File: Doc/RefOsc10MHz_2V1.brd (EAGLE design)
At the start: 90 x 70 mm, 77 parts, among them CON1 TYCO-AMP_USBUSB-B_SMT, CON11 MCX-J-P-X-RA-SM1, CON2 HEADER-2X5SMD, CON3 SD-73100-0105, CON4 AVR-ISP-6SMD, CON5 AVR-JTAG-10SMD, CON6 HEADER-2X3SMD, IC1 ATmega328-P, IC11 712-RXM-GNSS-TM-B, IC2 LC4032V_XXT44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

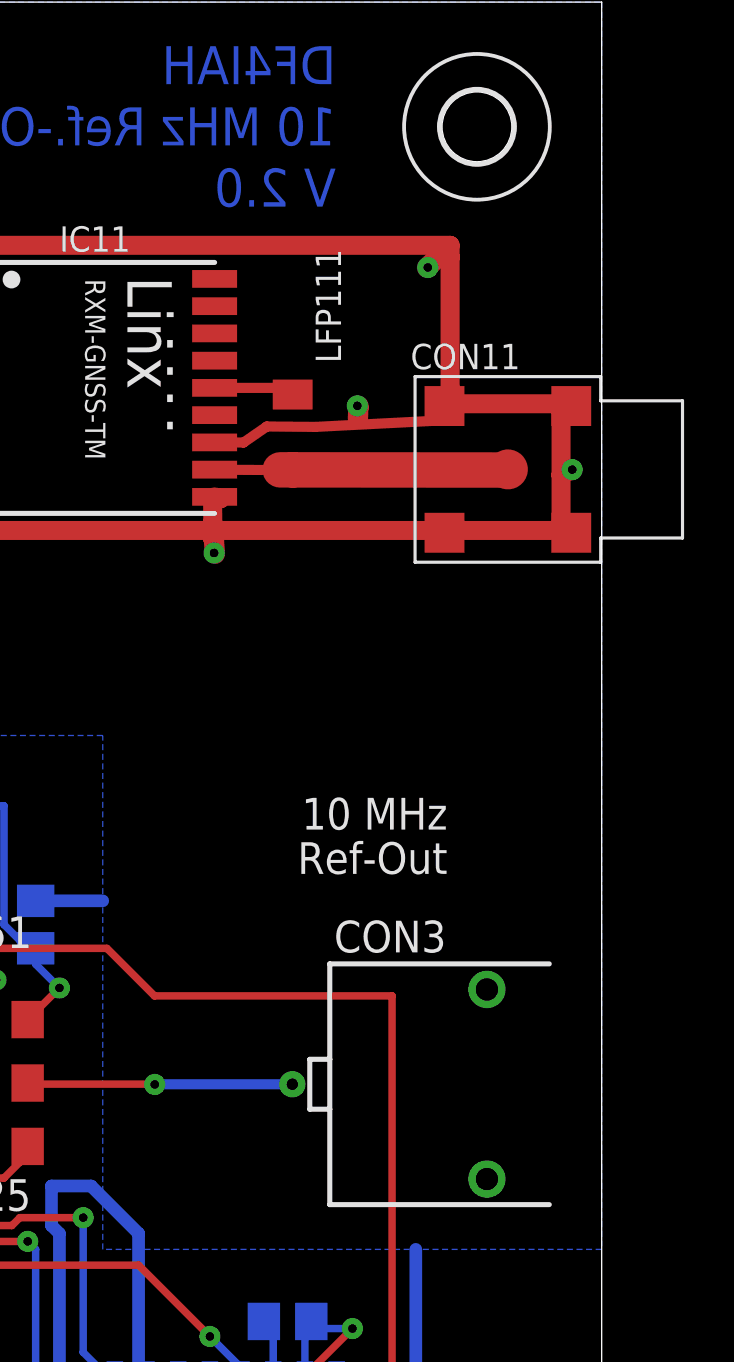
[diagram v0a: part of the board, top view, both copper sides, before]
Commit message: avr_DF4IAH_Bootloader - Doc - Eagle: V2.1 after manufacturing by PCB-Pool - findings to be fixed
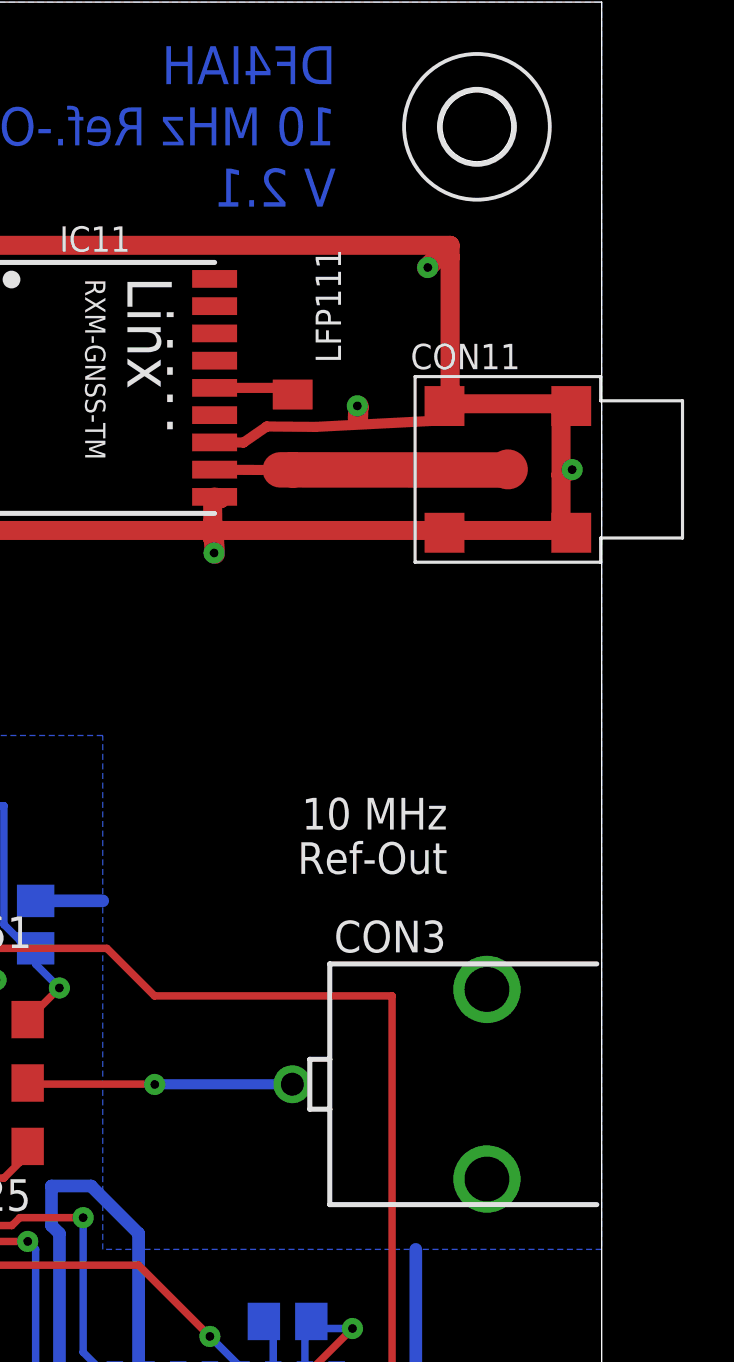
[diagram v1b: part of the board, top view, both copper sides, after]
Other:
- board text added: "DF4IAH 10 MHz Ref.-Osc. V 2.1"
- board text removed: "DF4IAH 10 MHz Ref.-Osc. V 2.0"
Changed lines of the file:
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@@
 <text x="79.347615625" y="65.017203125" size="1.524" layer="16" font="vector" ratio="18" distance="61" rot="MR0" align="center-left">DF4IAH
 10 MHz Ref.-Osc.
-V 2.0</text>
+V 2.1</text>
 <text x="6.35" y="10.16" size="1.27" layer="16" font="vector" ratio="20" distance="40" rot="MR0">Bot</text>
 <text x="2.54" y="10.16" size="1.27" layer="1" font="vector" ratio="20" distance="40">Top</text>
@@
 </element>
 <element name="CON6" library="df4iah" package="2X03SMD" value="HEADER-2X3SMD" x="13.97" y="62.23"/>
-<element name="CON3" library="df4iah" package="MOLEX_BNC-JACK-50R_SD-73100-0105" value="SD-73100-0105" x="90" y="26.62" smashed="yes" rot="R180">
+<element name="CON3" library="df4iah" package="MOLEX_BNC-JACK-50R_SD-73100-0105" value="SD-73100-0105" x="90" y="26.62" locked="yes" smashed="yes" rot="R180">
 <attribute name="OC_NEWARK" value="-" x="90" y="26.62" size="1.778" layer="27" rot="R180" display="off"/>
 <attribute name="MPN" value="SD-73100-0105" x="90" y="26.62" size="1.778" layer="27" rot="R180" display="off"/>
@@
 <via x="40.9575" y="63.5" extent="1-16" drill="0.35"/>
 <contactref element="CON3" pad="3"/>
-<contactref element="CON3" pad="2"/>
+<contactref element="CON3" pad="3"/>
 <contactref element="CON1" pad="4"/>
 <wire x1="18.875" y1="26" x2="15.375" y2="26" width="0.508" layer="1"/>
@@
 <wire x1="7.62" y1="44.1325" x2="7.62" y2="43.89" width="0.508" layer="1"/>
 <wire x1="11.43" y1="58.98" x2="11.43" y2="44.7675" width="0.508" layer="1"/>
+<contactref element="CON3" pad="2"/>
 </signal>
 <signal name="VCC" class="2">
@@
 <wire x1="67" y1="26.625" x2="66.99" y2="26.67" width="0.3" layer="1"/>
 <via x="72.084046875" y="26.6119875" extent="1-16" drill="0.35"/>
-<wire x1="77.6" y1="26.62" x2="72.084046875" y2="26.62" width="0.4064" layer="16"/>
 <wire x1="72.084046875" y1="26.62" x2="72.084046875" y2="26.6119875" width="0.4064" layer="16"/>
+<wire x1="72.084046875" y1="26.62" x2="77.6" y2="26.62" width="0.4064" layer="16"/>
 </signal>
 <signal name="N$44">

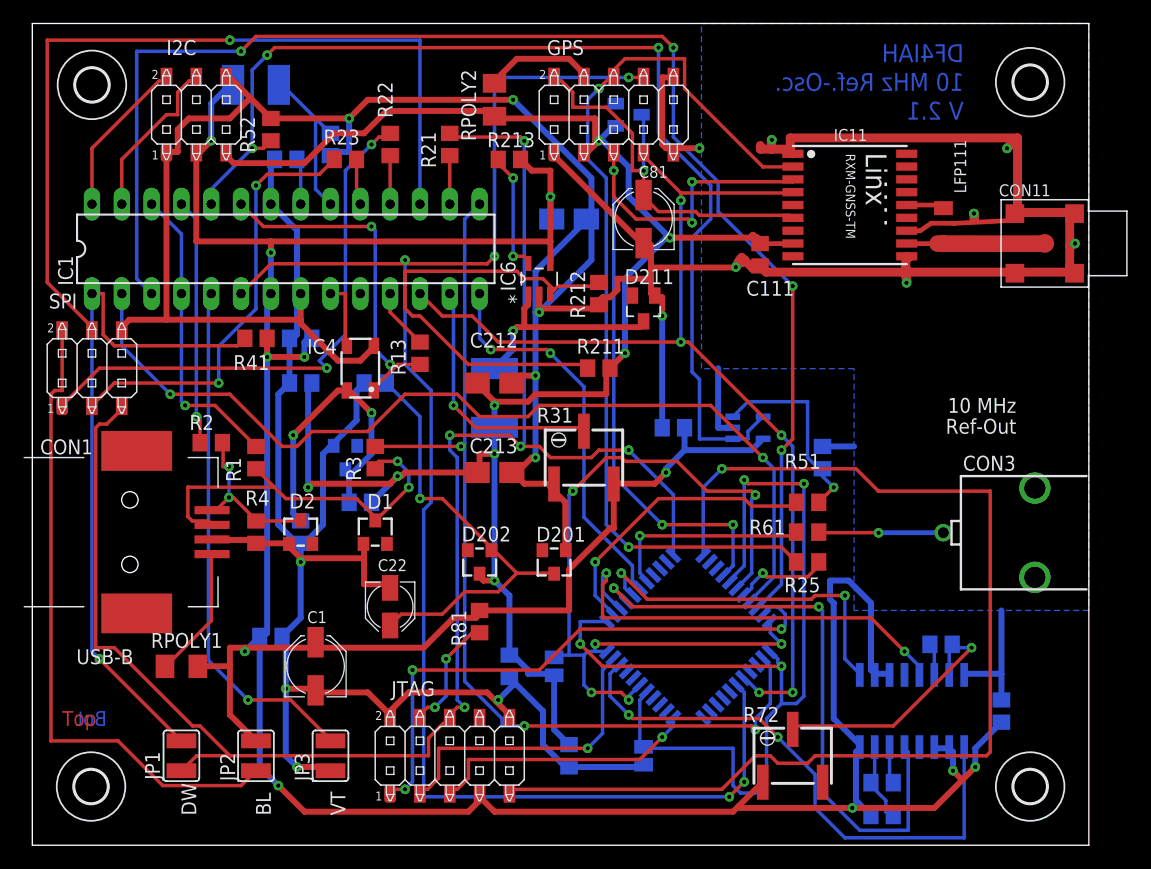
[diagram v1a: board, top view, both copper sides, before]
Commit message: avr_DF4IAH_Bootloader - Doc - Eagle: V2.1 after manufacturing by PCB-Pool - findings to be fixed (2) - BNC-Drills size doubled, Goldcap bigger than assumed, switching converter had wrong PIN assignment, now with grounded bottom layer
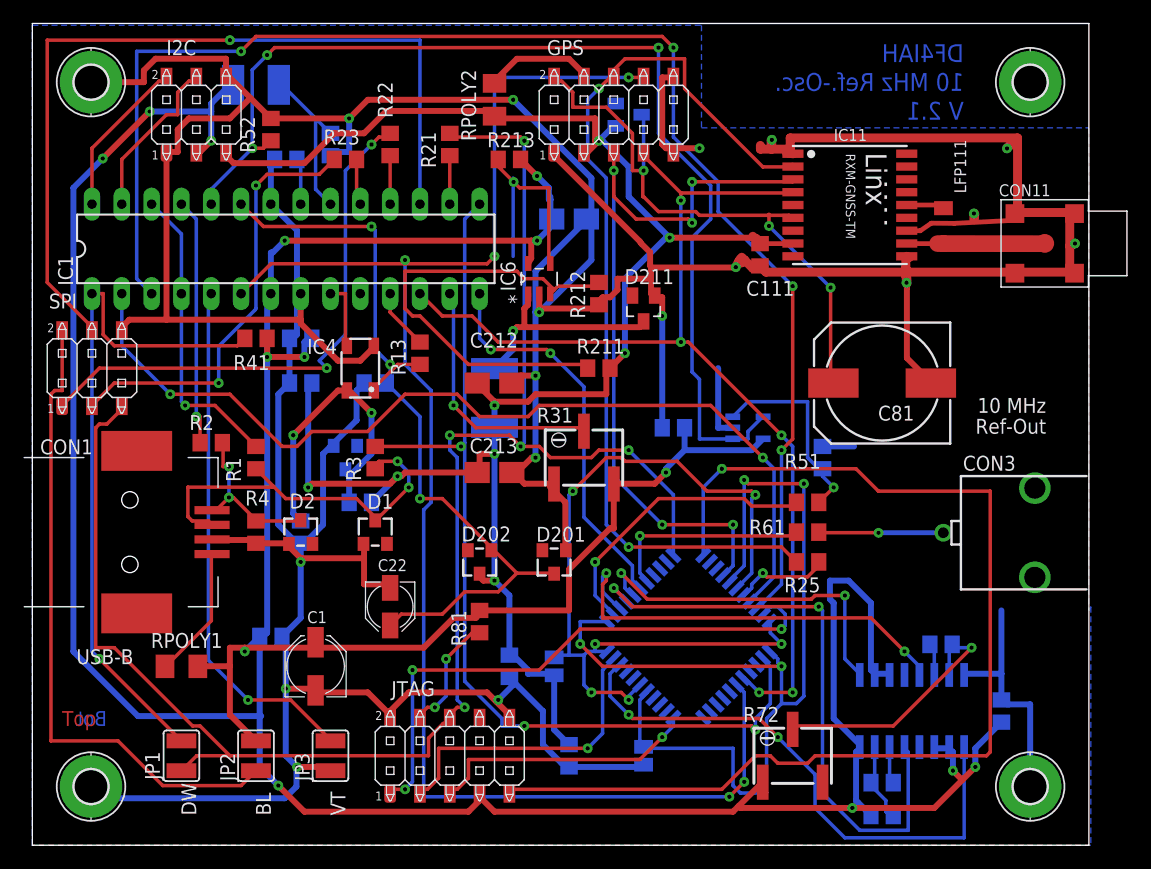
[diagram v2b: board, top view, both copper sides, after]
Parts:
- removed U$1, U$2, U$3, U$4: (no value), holes:2,8
- added H1, H2, H3, H4: MOUNT-PAD-ROUND2.8, holes:2,8-PAD
- C81: device rcl:PANASONIC_C -> rcl:140CLH-1010
- moved C81 24.7 mm to (72.4, 39.4), turned to 180 degrees
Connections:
- net EN: now also IC6.4; no longer IC6.5
- net GND: now also H1.B2,8, H2.B2,8, H3.B2,8, H4.B2,8
- net VCC: now also IC6.5; no longer IC6.4
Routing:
- net VCC: track 296.4 -> 351.1 mm, vias 11 -> 14
- net GND: track 450.6 -> 503.4 mm
- net GPS_VBACKUP: track 34.6 -> 51.4 mm, vias 1 -> 3
- net EN: track 10.7 -> 19.9 mm, vias 2 -> 1

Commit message: avr_DF4IAH_Bootloader - Doc - Eagle: V2.1 after manufacturing by PCB-Pool - findings to be fixed (3) - take big C211 from bottom to top.
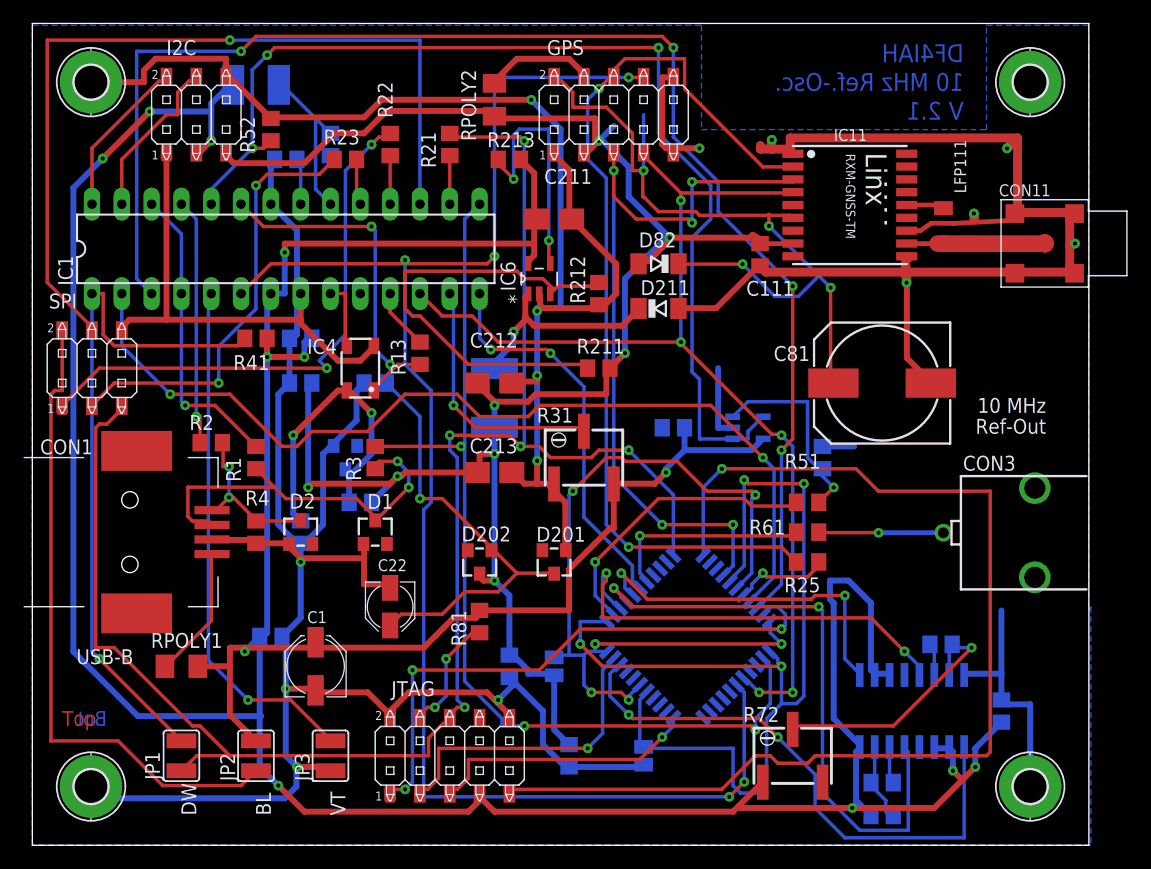
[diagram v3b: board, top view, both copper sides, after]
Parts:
- D211, D82: value CRS08 -> CRS80; device diode:SOT23 -> diode:SOD80C
- moved D82 13.0 mm to (53.3, 49.5), flipped to the top, turned to 180 degrees
- moved D211 1.27 mm to (53.3, 45.7), turned to 0 degrees
- moved C211 1.27 mm to (44.5, 53.3), flipped to the top, turned to 180 degrees
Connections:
- net +3V3: now also D82.A; no longer D82.1
- net GND: now also D211.A; no longer D211.1
- net GPS_VBACKUP: now also D82.C; no longer D82.3
- net SW: now also D211.C; no longer D211.3
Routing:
- net GND: track 503.4 -> 459.1 mm, vias 17 -> 14
- net GPS_VBACKUP: track 51.4 -> 65.0 mm, vias 3 -> 4
- net +3V3: track 156.9 -> 160.4 mm
- net EN: track 19.9 -> 21.5 mm, vias 1 -> 2
- net VCC: track 351.1 -> 350.1 mm, vias 14 -> 12

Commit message: avr_DF4IAH_Bootloader - Doc - Eagle: V2.1 after manufacturing by PCB-Pool - findings to be fixed (4) - change R81 from 1k to 150Ohm, 3.3V regulator corrected.
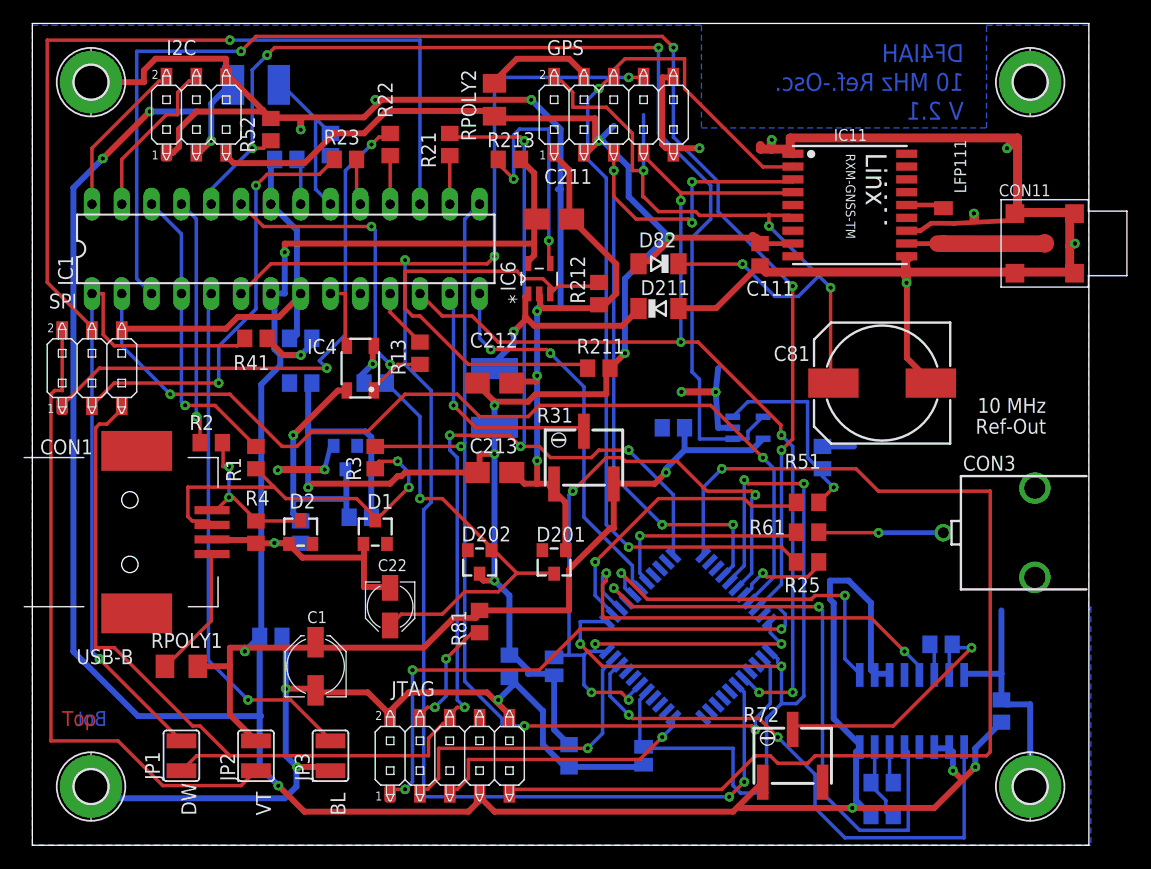
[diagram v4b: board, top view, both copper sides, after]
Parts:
- R211: value 10k -> 45.3k
- R81: value 1k -> 150
- moved R221 1.27 mm to (27.9, 27.9)
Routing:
- net GND: track 459.1 -> 420.8 mm, vias 14 -> 21
- net +3V3: track 160.4 -> 169.7 mm, vias 8 -> 7
- net +3V0: track 26.4 -> 22.7 mm, vias 2 -> 1
- net VCC: track 350.1 -> 350.9 mm, vias 12 -> 11
